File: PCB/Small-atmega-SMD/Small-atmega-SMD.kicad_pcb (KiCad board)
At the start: 2 copper layers, 65.1 x 96.9 mm, 31 parts, among them J1 Daisy port out, J2 ICSP_ISP6, J3 UART, J4 Daisy port in, K1 HYC77-TF09-200, U1 PC817C-S, U2 ATmega328P-AU, U3 SE5218, U4 TXB0104PWR, Y1 Resonator_GND2

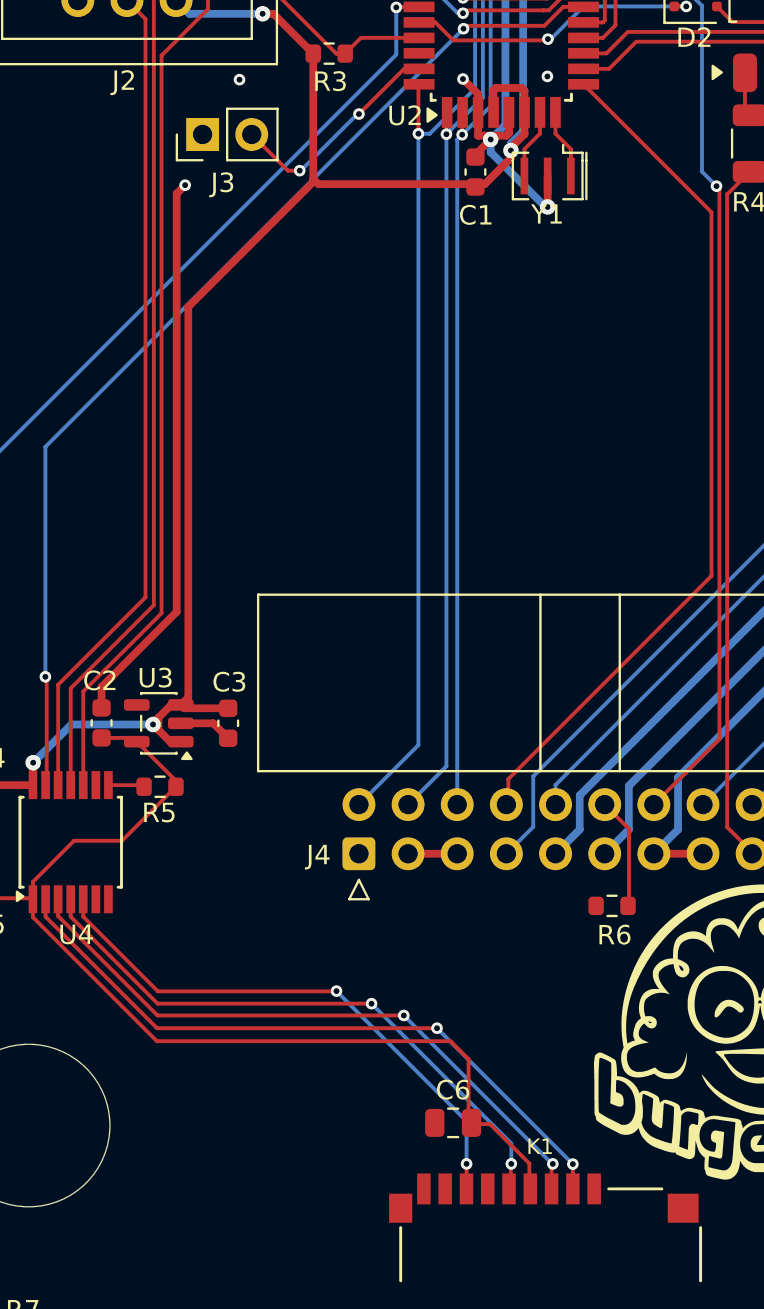
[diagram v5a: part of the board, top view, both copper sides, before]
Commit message: Small caps fixes
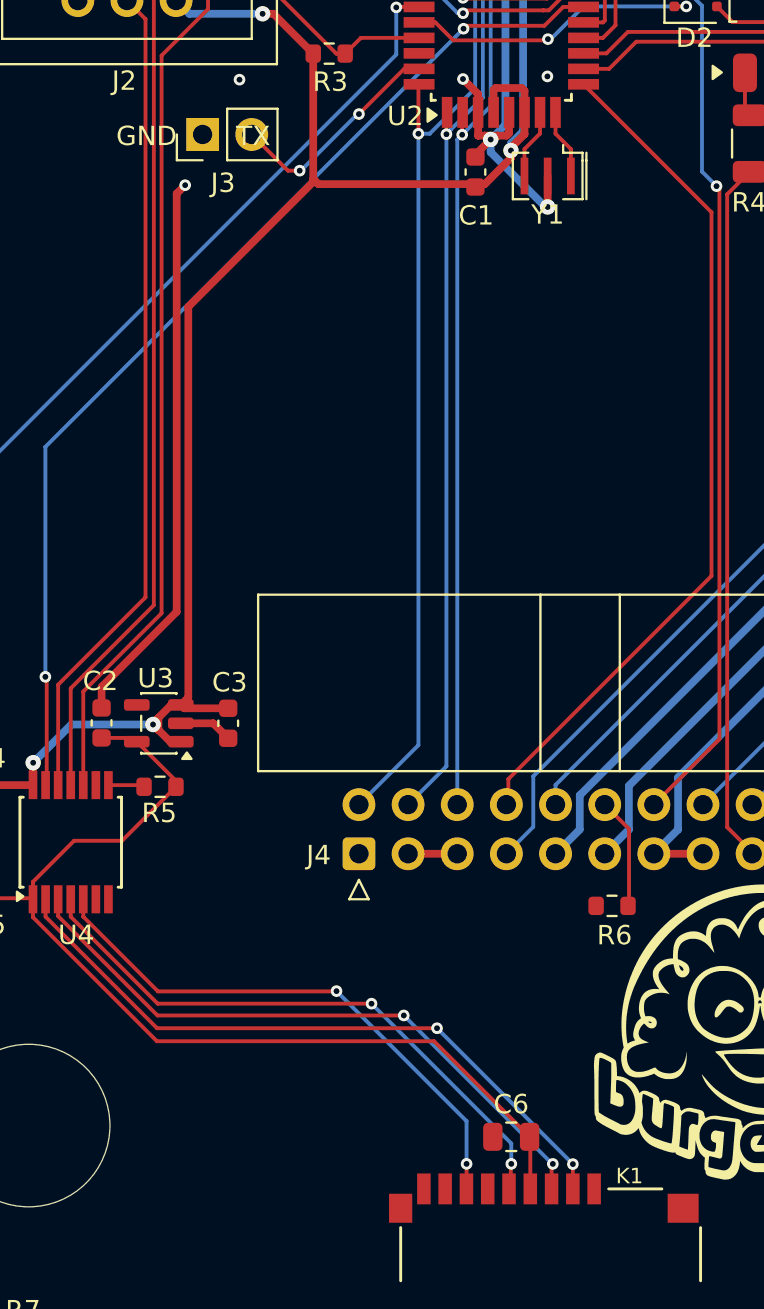
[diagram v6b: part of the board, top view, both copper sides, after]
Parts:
- moved C6 3.09 mm to (130.1, 124.6)
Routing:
- net 3V3: track 52.1 -> 51.0 mm
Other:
- board text added: "GND TX"
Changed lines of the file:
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@@
 		(at 132.1562 135.0518)
 		(property "Reference" "K1"
-			(at -0.5444 -9.9248 0)
+			(at 4.0738 -8.4118 0)
 			(layer "F.SilkS")
 			(effects
@@
 	(footprint "Capacitor_SMD:C_0805_2012Metric"
 		(layer "F.Cu")
-		(at 127.12 123.89)
+		(at 130.12 124.61)
 		(descr "Capacitor SMD 0805 (2012 Metric), square (rectangular) end terminal, IPC_7351 nominal, (Body size source: IPC-SM-782 page 76, https://www.pcb-3d.com/wordpress/wp-content/uploads/ipc-sm-782a_amendment_1_and_2.pdf, https://docs.google.com/spreadsheets/d/1BsfQQcO9C6DZCsRaXUlFlo91Tg2WpOkGARC1WS5S8t0/edit?usp=sharing), generated with kicad-footprint-generator")
 		(tags "capacitor")
@@
 		(layer "Edge.Cuts")
 	)
+	(gr_text "GND       TX"
+		(at 109.7 73.48 0)
+		(layer "F.SilkS")
+		(effects
+			(font
+				(size 1 1)
+				(thickness 0.1)
+			)
+			(justify left bottom)
+		)
+	)
 	(gr_text "BurgerDisk - CC BY-SA\n© Colin Leroy-Mira 2026\nhttps://github.com/colinleroy/BurgerDisk"
 		(at 155.9306 89.662 0)
@@
 	)
 	(segment
-		(start 127.9144 120.5992)
-		(end 127.9144 122.3264)
-		(width 0.2)
-		(layer "F.Cu")
-		(net 39)
-	)
-	(segment
 		(start 112.795 106.52)
 		(end 110.005 109.31)
@@
 	)
 	(segment
-		(start 127.9144 122.3264)
-		(end 127.9144 123.952)
+		(start 103.1234 112.281)
+		(end 105.3508 112.281)
 		(width 0.2)
 		(layer "F.Cu")
@@
 	)
 	(segment
-		(start 103.1234 112.281)
-		(end 105.3508 112.281)
+		(start 126.13 119.67)
+		(end 131.07 124.61)
 		(width 0.2)
 		(layer "F.Cu")
@@
 	)
 	(segment
-		(start 105.4042 113.2642)
-		(end 111.81 119.67)
+		(start 105.4042 111.4324)
+		(end 105.4042 112.3344)
 		(width 0.2)
 		(layer "F.Cu")
@@
 	)
 	(segment
-		(start 105.4042 111.4324)
-		(end 105.4042 112.3344)
+		(start 105.4042 112.3344)
+		(end 105.4042 113.2642)
 		(width 0.2)
 		(layer "F.Cu")
@@
 	)
 	(segment
-		(start 129.02167 123.952)
-		(end 131.058835 125.989165)
+		(start 111.81 119.67)
+		(end 126.13 119.67)
 		(width 0.2)
 		(layer "F.Cu")
@@
 	)
 	(segment
-		(start 111.81 119.67)
-		(end 126.9852 119.67)
+		(start 131.1062 124.6462)
+		(end 131.07 124.61)
 		(width 0.2)
 		(layer "F.Cu")
@@
 	)
 	(segment
-		(start 131.058835 125.989165)
-		(end 131.058835 127.254435)
+		(start 131.1062 127.3018)
+		(end 131.1062 124.6462)
 		(width 0.2)
 		(layer "F.Cu")
@@
 	)
 	(segment
-		(start 105.4042 112.3344)
-		(end 105.4042 113.2642)
-		(width 0.2)
-		(layer "F.Cu")
-		(net 39)
-	)
-	(segment
 		(start 110.7694 104.1908)
 		(end 112.795 106.2164)
@@
 	)
 	(segment
-		(start 127.9144 123.952)
-		(end 129.02167 123.952)
-		(width 0.2)
-		(layer "F.Cu")
-		(net 39)
-	)
-	(segment
-		(start 126.9852 119.67)
-		(end 127.9144 120.5992)
+		(start 105.4042 113.2642)
+		(end 111.81 119.67)
 		(width 0.2)
 		(layer "F.Cu")

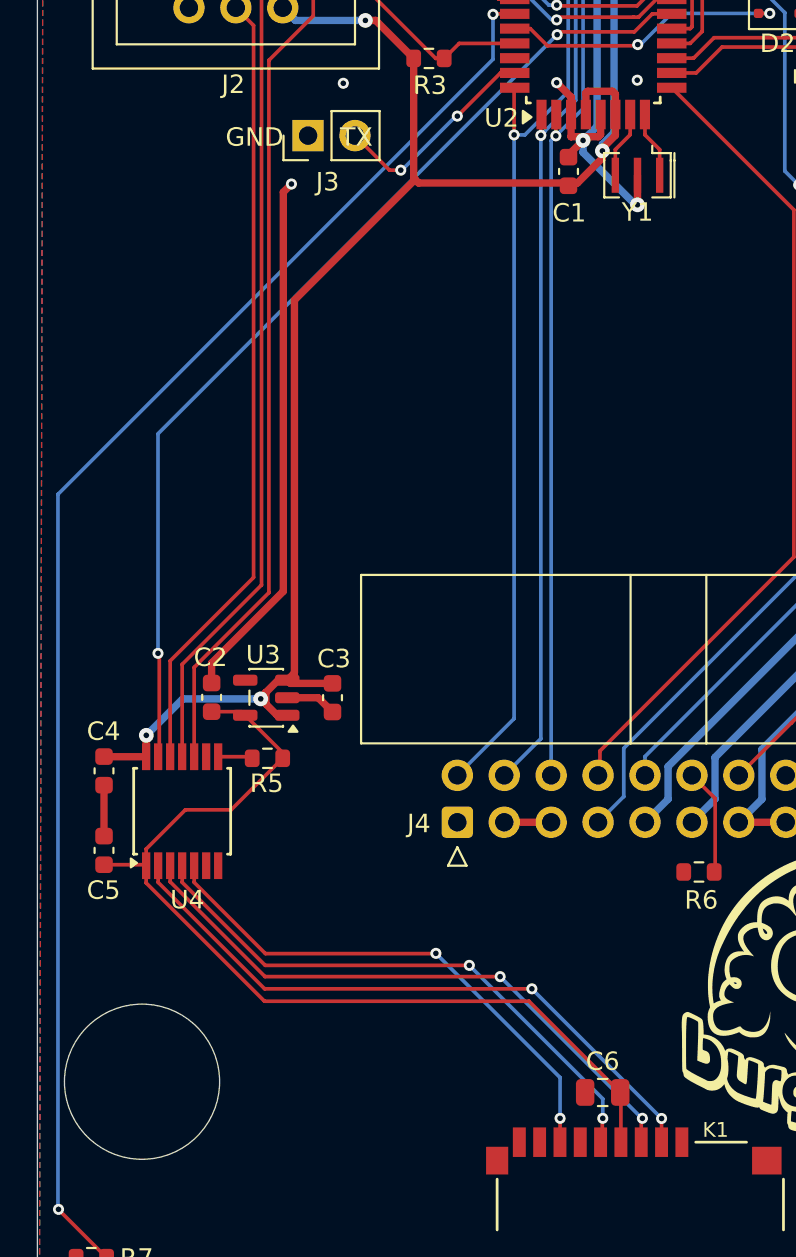
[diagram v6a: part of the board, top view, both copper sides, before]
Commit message: fatter traces
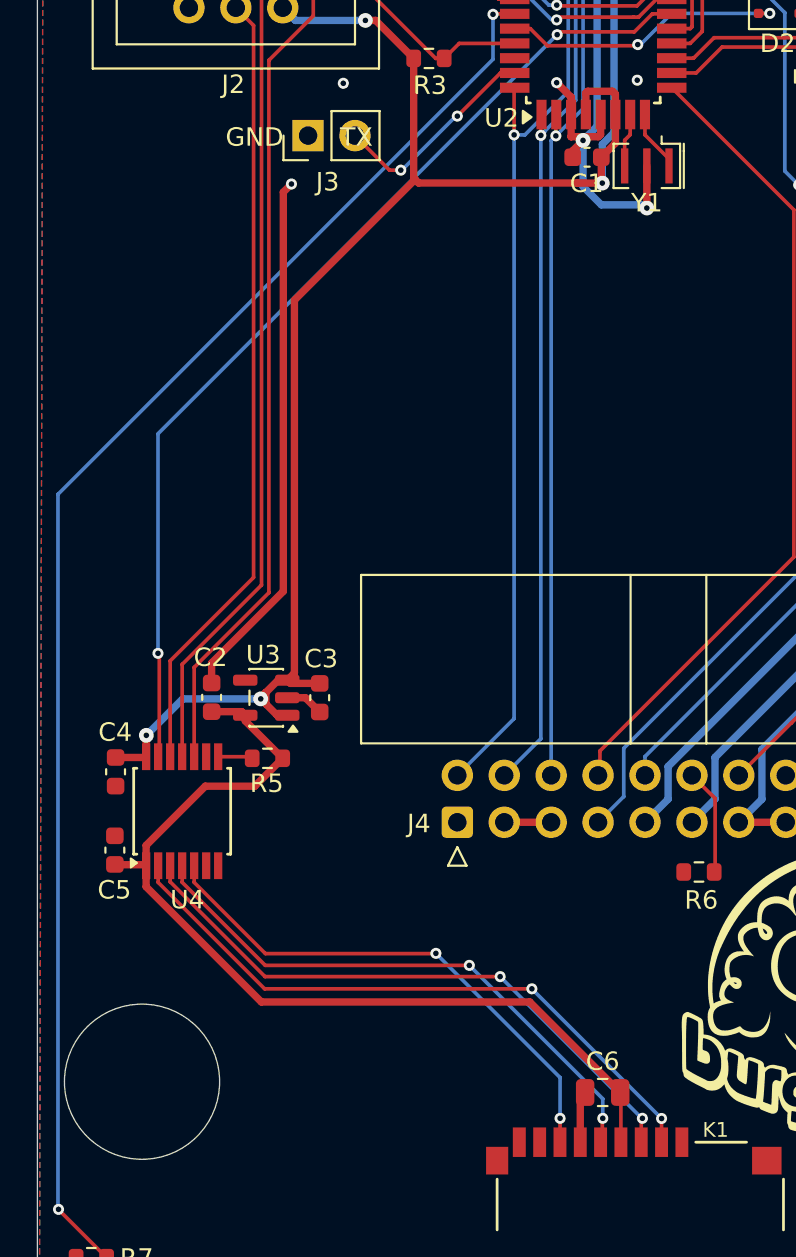
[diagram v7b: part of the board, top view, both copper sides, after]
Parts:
- moved C1 1.26 mm to (129.3, 74.0), turned to 180 degrees
- moved Y1 0.72 mm to (132.5, 74.5)
- moved C3 0.69 mm to (114.8, 103.2)
- moved C4 0.63 mm to (103.8, 107.2)
- moved C5 0.59 mm to (103.7, 111.5)
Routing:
- net GND: track 67.4 -> 69.1 mm
- net 5V_burgerDisk: track 107.9 -> 109.5 mm
- net Net-(U2-XTAL1/PB6): track 3.62 -> 2.91 mm

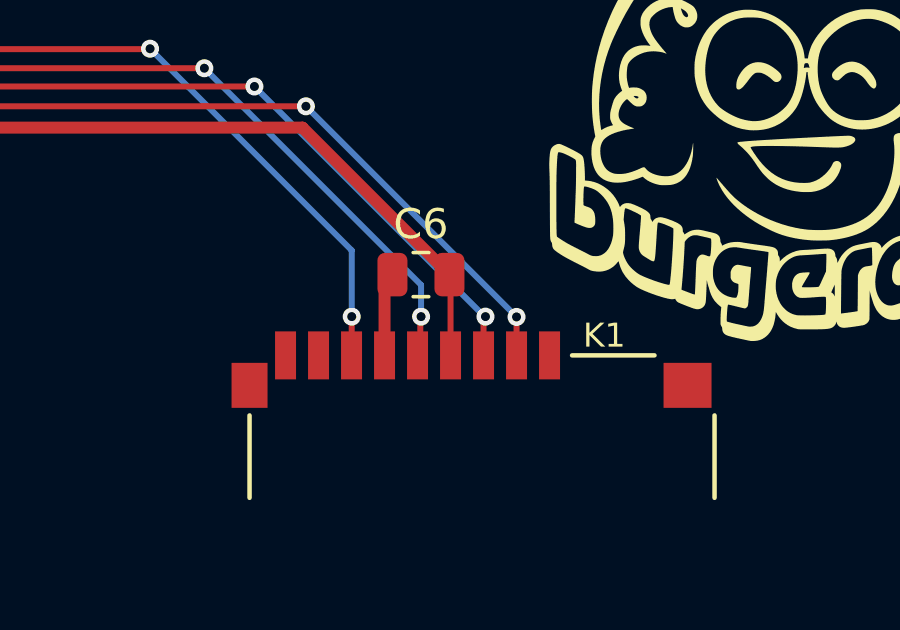
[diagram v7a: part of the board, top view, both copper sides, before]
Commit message: Enable teardrops
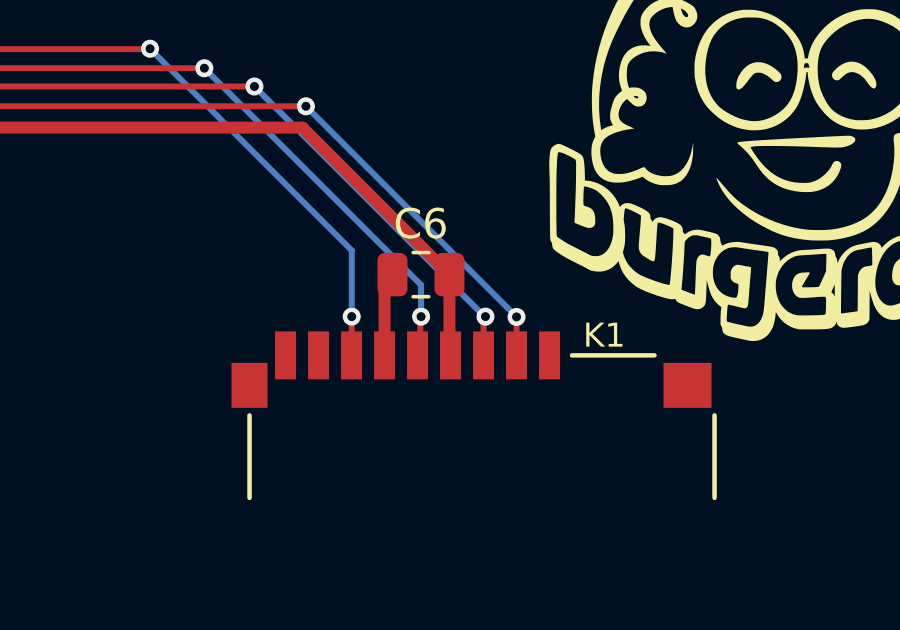
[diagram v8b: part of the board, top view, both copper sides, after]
